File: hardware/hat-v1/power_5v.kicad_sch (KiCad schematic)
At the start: 22 parts, among them Q3 CSD17578Q3A, Q7 BSS138, U3 LMR33640DDDAR, U4 LM74700QDBVRQ1

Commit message: HAT v1 schematic: apply adversarial review (power + digital/security/DFM)
AUTO-ON above buck EN window, BENCH no longer blocks power-off, OVP moved
to 19.2 V with input damper, Tier A parts DNP for JLC, debug links
removable for production, antenna short limited, stock footprints where
available, cap ratings/DC-bias fixes, CONSOLE_TX/RX naming.

Co-Authored-By: Claude Opus 5.5 <noreply@anthropic.com>
Claude-Session: https://claude.ai/code/session_01MLRuxTEmuMV82xcNLE62jW
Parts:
- C10: value 10u 35V X5R -> 10u 50V X7R; footprint Capacitor_SMD:C_1206_3216Metric -> Capacitor_SMD:C_1210_3225Metric
- C18: value 100n 16V -> 220n 25V X7R; footprint Capacitor_SMD:C_0402_1005Metric -> Capacitor_SMD:C_0603_1608Metric
- D3: footprint LED_SMD:LED_0603_1608Metric -> LED_SMD:LED_0402_1005Metric
- L1: footprint Inductor_SMD:L_Coilcraft_XGL4030 -> Inductor_SMD:L_Coilcraft_XxL4030
- Q3: footprint batman:TI_VSON-CLIP-8_3.3x3.3mm -> Package_SON:VSON-8_3.3x3.3mm_P0.65mm_NexFET
- R13: value 100k 1% -> 100k 0.5%
- R14: value 24.0k 1% -> 24.0k 0.5%
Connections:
- net 5V_PI: no longer Q3.6 (D), Q3.7 (D), Q3.8 (D), Q3.9 (D)
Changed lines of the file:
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@@
   (symbol (lib_id "batman:C") (at 77.47 26.67 0) (unit 1) (in_bom yes) (on_board yes) (dnp no)
     (property "Reference" "C10" (at 77.47 24.13 0) (effects (font (size 1.27 1.27)) (justify bottom)))
-    (property "Value" "10u 35V X5R" (at 77.47 29.21 0) (effects (font (size 1.27 1.27)) (justify top)))
-    (property "Footprint" "Capacitor_SMD:C_1206_3216Metric" (at 77.47 26.67 0) (effects (font (size 1.27 1.27)) hide))
+    (property "Value" "10u 50V X7R" (at 77.47 29.21 0) (effects (font (size 1.27 1.27)) (justify top)))
+    (property "Footprint" "Capacitor_SMD:C_1210_3225Metric" (at 77.47 26.67 0) (effects (font (size 1.27 1.27)) hide))
     (property "Datasheet" "" (at 77.47 26.67 0) (effects (font (size 1.27 1.27)) hide))
     (property "MPN" "" (at 77.47 26.67 0) (effects (font (size 1.27 1.27)) hide))
@@
     (property "Reference" "L1" (at 201.93 24.13 0) (effects (font (size 1.27 1.27)) (justify bottom)))
     (property "Value" "3.3uH Isat>=5.5A" (at 201.93 29.21 0) (effects (font (size 1.27 1.27)) (justify top)))
-    (property "Footprint" "Inductor_SMD:L_Coilcraft_XGL4030" (at 201.93 26.67 0) (effects (font (size 1.27 1.27)) hide))
+    (property "Footprint" "Inductor_SMD:L_Coilcraft_XxL4030" (at 201.93 26.67 0) (effects (font (size 1.27 1.27)) hide))
     (property "Datasheet" "" (at 201.93 26.67 0) (effects (font (size 1.27 1.27)) hide))
     (property "MPN" "XGL4030-332MEC" (at 201.93 26.67 0) (effects (font (size 1.27 1.27)) hide))
@@
   (symbol (lib_id "batman:R") (at 102.87 49.53 0) (unit 1) (in_bom yes) (on_board yes) (dnp no)
     (property "Reference" "R13" (at 102.87 46.99 0) (effects (font (size 1.27 1.27)) (justify bottom)))
-    (property "Value" "100k 1%" (at 102.87 52.07 0) (effects (font (size 1.27 1.27)) (justify top)))
+    (property "Value" "100k 0.5%" (at 102.87 52.07 0) (effects (font (size 1.27 1.27)) (justify top)))
     (property "Footprint" "Resistor_SMD:R_0402_1005Metric" (at 102.87 49.53 0) (effects (font (size 1.27 1.27)) hide))
     (property "Datasheet" "" (at 102.87 49.53 0) (effects (font (size 1.27 1.27)) hide))
@@
   (symbol (lib_id "batman:R") (at 132.08 49.53 0) (unit 1) (in_bom yes) (on_board yes) (dnp no)
     (property "Reference" "R14" (at 132.08 46.99 0) (effects (font (size 1.27 1.27)) (justify bottom)))
-    (property "Value" "24.0k 1%" (at 132.08 52.07 0) (effects (font (size 1.27 1.27)) (justify top)))
+    (property "Value" "24.0k 0.5%" (at 132.08 52.07 0) (effects (font (size 1.27 1.27)) (justify top)))
     (property "Footprint" "Resistor_SMD:R_0402_1005Metric" (at 132.08 49.53 0) (effects (font (size 1.27 1.27)) hide))
     (property "Datasheet" "" (at 132.08 49.53 0) (effects (font (size 1.27 1.27)) hide))
@@
   (symbol (lib_id "batman:C") (at 165.1 62.23 0) (unit 1) (in_bom yes) (on_board yes) (dnp no)
     (property "Reference" "C18" (at 165.1 59.69 0) (effects (font (size 1.27 1.27)) (justify bottom)))
-    (property "Value" "100n 16V" (at 165.1 64.77 0) (effects (font (size 1.27 1.27)) (justify top)))
-    (property "Footprint" "Capacitor_SMD:C_0402_1005Metric" (at 165.1 62.23 0) (effects (font (size 1.27 1.27)) hide))
+    (property "Value" "220n 25V X7R" (at 165.1 64.77 0) (effects (font (size 1.27 1.27)) (justify top)))
+    (property "Footprint" "Capacitor_SMD:C_0603_1608Metric" (at 165.1 62.23 0) (effects (font (size 1.27 1.27)) hide))
     (property "Datasheet" "" (at 165.1 62.23 0) (effects (font (size 1.27 1.27)) hide))
     (property "MPN" "" (at 165.1 62.23 0) (effects (font (size 1.27 1.27)) hide))
@@
     (property "Reference" "Q3" (at 199.39 59.69 0) (effects (font (size 1.27 1.27)) (justify left bottom)))
     (property "Value" "CSD17578Q3A" (at 199.39 71.12 0) (effects (font (size 1.27 1.27)) (justify left top)))
-    (property "Footprint" "batman:TI_VSON-CLIP-8_3.3x3.3mm" (at 204.47 64.77 0) (effects (font (size 1.27 1.27)) hide))
+    (property "Footprint" "Package_SON:VSON-8_3.3x3.3mm_P0.65mm_NexFET" (at 204.47 64.77 0) (effects (font (size 1.27 1.27)) hide))
     (property "Datasheet" "" (at 204.47 64.77 0) (effects (font (size 1.27 1.27)) hide))
     (property "MPN" "CSD17578Q3A" (at 204.47 64.77 0) (effects (font (size 1.27 1.27)) hide))
@@
     (pin "4")
     (pin "5")
-    (pin "6")
-    (pin "7")
-    (pin "8")
-    (pin "9")
     (pin "1")
     (pin "2")
@@
     (property "Reference" "D3" (at 66.04 80.01 0) (effects (font (size 1.27 1.27)) (justify bottom)))
     (property "Value" "GREEN" (at 66.04 85.09 0) (effects (font (size 1.27 1.27)) (justify top)))
-    (property "Footprint" "LED_SMD:LED_0603_1608Metric" (at 66.04 82.55 0) (effects (font (size 1.27 1.27)) hide))
+    (property "Footprint" "LED_SMD:LED_0402_1005Metric" (at 66.04 82.55 0) (effects (font (size 1.27 1.27)) hide))
     (property "Datasheet" "" (at 66.04 82.55 0) (effects (font (size 1.27 1.27)) hide))
     (property "MPN" "" (at 66.04 82.55 0) (effects (font (size 1.27 1.27)) hide))

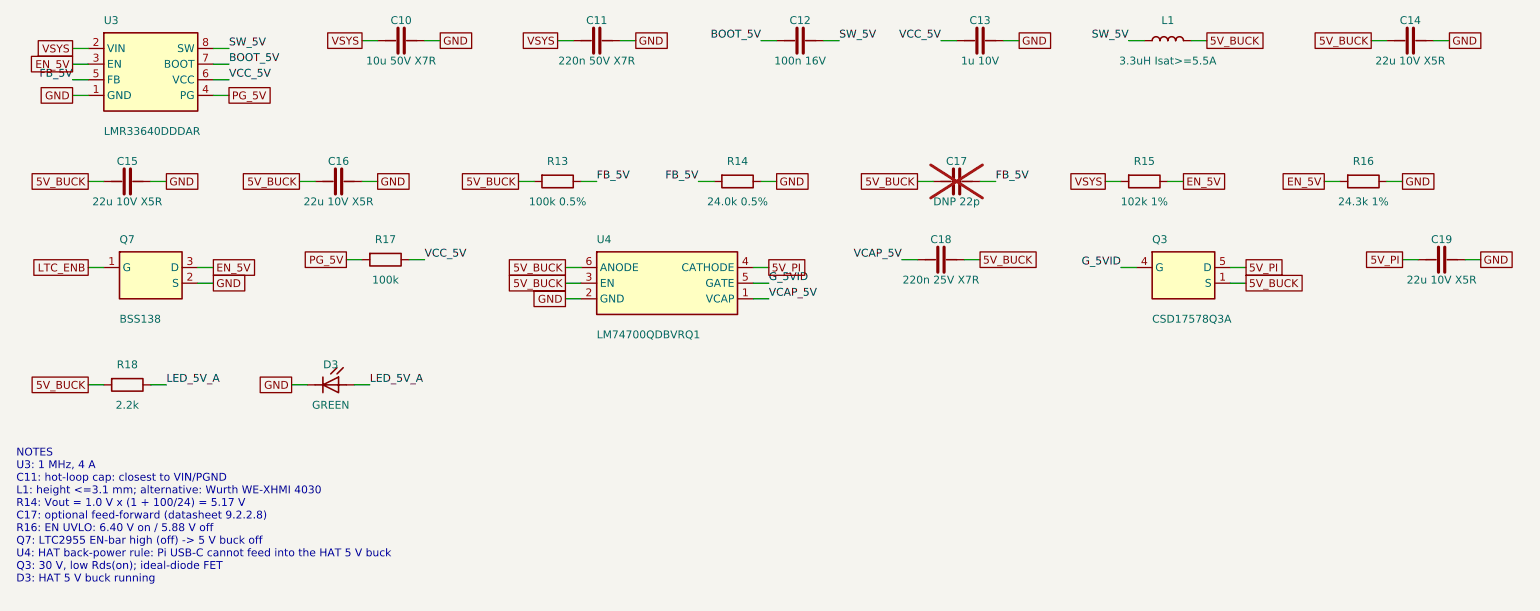
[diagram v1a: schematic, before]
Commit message: HAT v1 layout v2: placement plan, G0 sketch checker and KiCad escape proof; add C34
Redo of the HAT v1 placement (schematic frozen except C34), after the
power-distribution close-out turned into whack-a-mole (HANDOFF §7).

- layout-v2/PLAN.md: acceptance criteria (IR-drop budgets, hot loops,
  bypass table, keep-outs, noise distances, sensitive nodes, thermal),
  zone plan A and three adversarial review rounds with responses (§6-§9).
- sketch.json + sketch.py (G0): coordinate-level placement checked with
  real courtyards/pads exported by export_fp.py (fpdata.json).
- escape.py + escape.json (G0.5): experiment board from the real
  footprints under JLC 2 oz outer rules (0.2/0.21, via 0.3/0.8); planned
  pours, hand-planned escapes, GND vias, deterministic A* routing,
  KiCad DRC and neck widths (erosion + pad-entry exemption).
- gen/design.py: C34 2.2 nF EN_5V -> GND at U3 EN (the EN divider moves
  next to Q7; EN_5V becomes a ~30 mm In2 node). User-approved.

Test results (escape proof, KiCad 7.0.11 pcbnew in WSL, 2026-09-29):
- 31 nets routed, 0 unconnected on routed nets, 52 GND vias placed,
  no dangling vias. DRC clearance: 3 known items (VSON pad gap 0.14 x2,
  a 0.19 router-grid track); annular 0.15 in 41 footprint thermal vias.
- Main-path necks: VBAT 2.45, VSYS 1.95/1.19, 5V_BUCK 1.71, 5V_PI 0.96
  (+B), 3V3_BUCK 1.30 mm; In2 5V_PI feed 1.00 mm (to widen in G1).
- gen/check.py: PASS, 0 errors, 0 warnings, 522 pins vs netlist.
Not done: G1 place-only on the real board, Z4-Z8 detail, U3 thermal
calc, footprint annular/VSON fixes, H5/H6 part.

Co-Authored-By: Claude Opus 5.5 <noreply@anthropic.com>
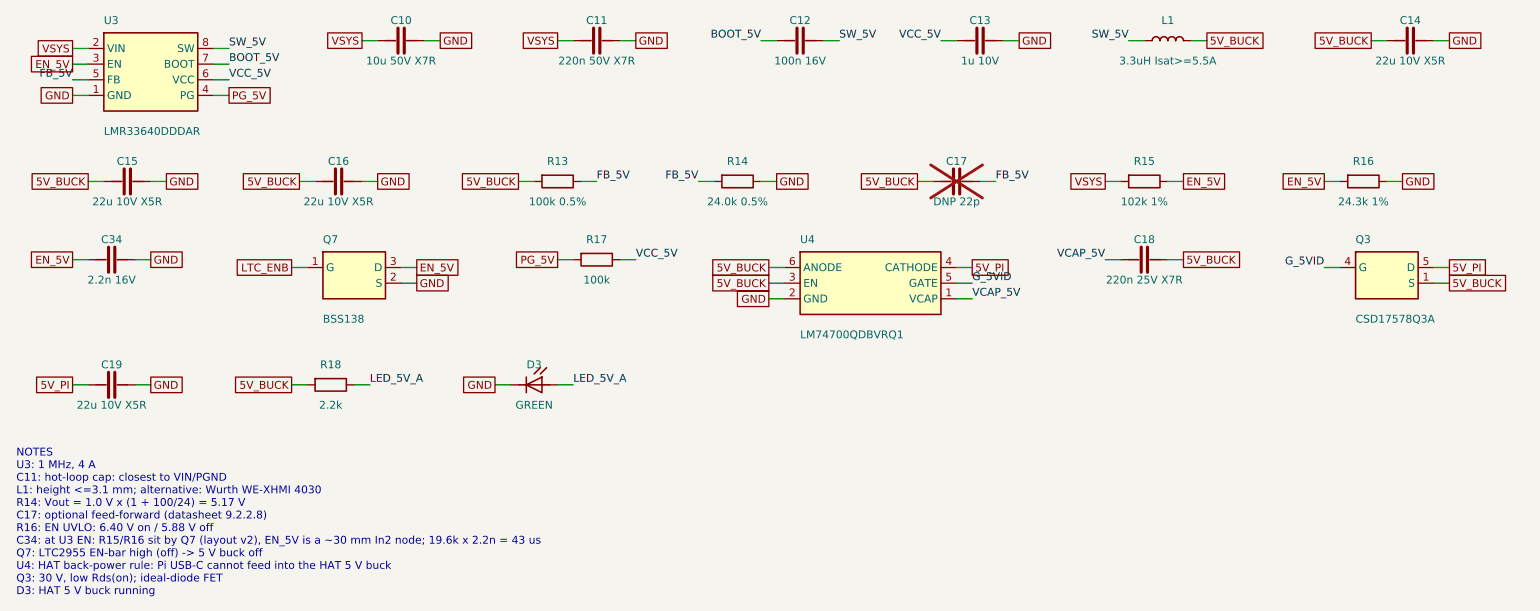
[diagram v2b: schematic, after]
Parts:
- added C34: 2.2n 16V, Capacitor_SMD:C_0402_1005Metric, symbol batman:C
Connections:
- net EN_5V: now also C34.1
- net GND: now also C34.2
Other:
- note added: "NOTES U3: 1 MHz, 4 A C11: hot-loop cap: closest to VIN/PGND L1: height <=3.1 mm; alternative: Wurth WE-XHMI 4030 R14: Vout = 1.0 V x (1 + 100/24) = 5.17 V C17: optional feed-forward (datasheet 9.2.2.8) R16: EN UVLO: 6.40 V on / 5.88 V off C34: at U3 EN: R15/R16 sit by Q7 (layout v2), EN_5V is a ~30 mm In2 node; 19.6k x 2.2n = 43 us Q7: LTC2955 EN-bar high (off) -> 5 V buck off U4: HAT back-power 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"
- note removed: "NOTES U3: 1 MHz, 4 A C11: hot-loop cap: closest to VIN/PGND L1: height <=3.1 mm; alternative: Wurth WE-XHMI 4030 R14: Vout = 1.0 V x (1 + 100/24) = 5.17 V C17: optional feed-forward (datasheet 9.2.2.8) R16: EN UVLO: 6.40 V on / 5.88 V off Q7: LTC2955 EN-bar high (off) -> 5 V buck off U4: HAT back-power rule: Pi USB-C cannot feed into the HAT 5 V buck Q3: 30 V, low Rds(on); ideal-diode FET D3: HAT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"
- moved on the sheet: C18, C19, D3, Q3, Q7, R17, R18, U4
